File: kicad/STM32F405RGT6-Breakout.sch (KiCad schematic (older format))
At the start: 58 parts, among them J1 USB_C_Receptacle_USB2.0, J2 PWR OUT, J3 SWD/JTAG, J4 USART6, J5 SPI1, J6 I2C1, J7 I2C2, Q1 Si2301CDS, SW1 TS-1187A-B-A-B, SW2 TS-1187A-B-A-B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

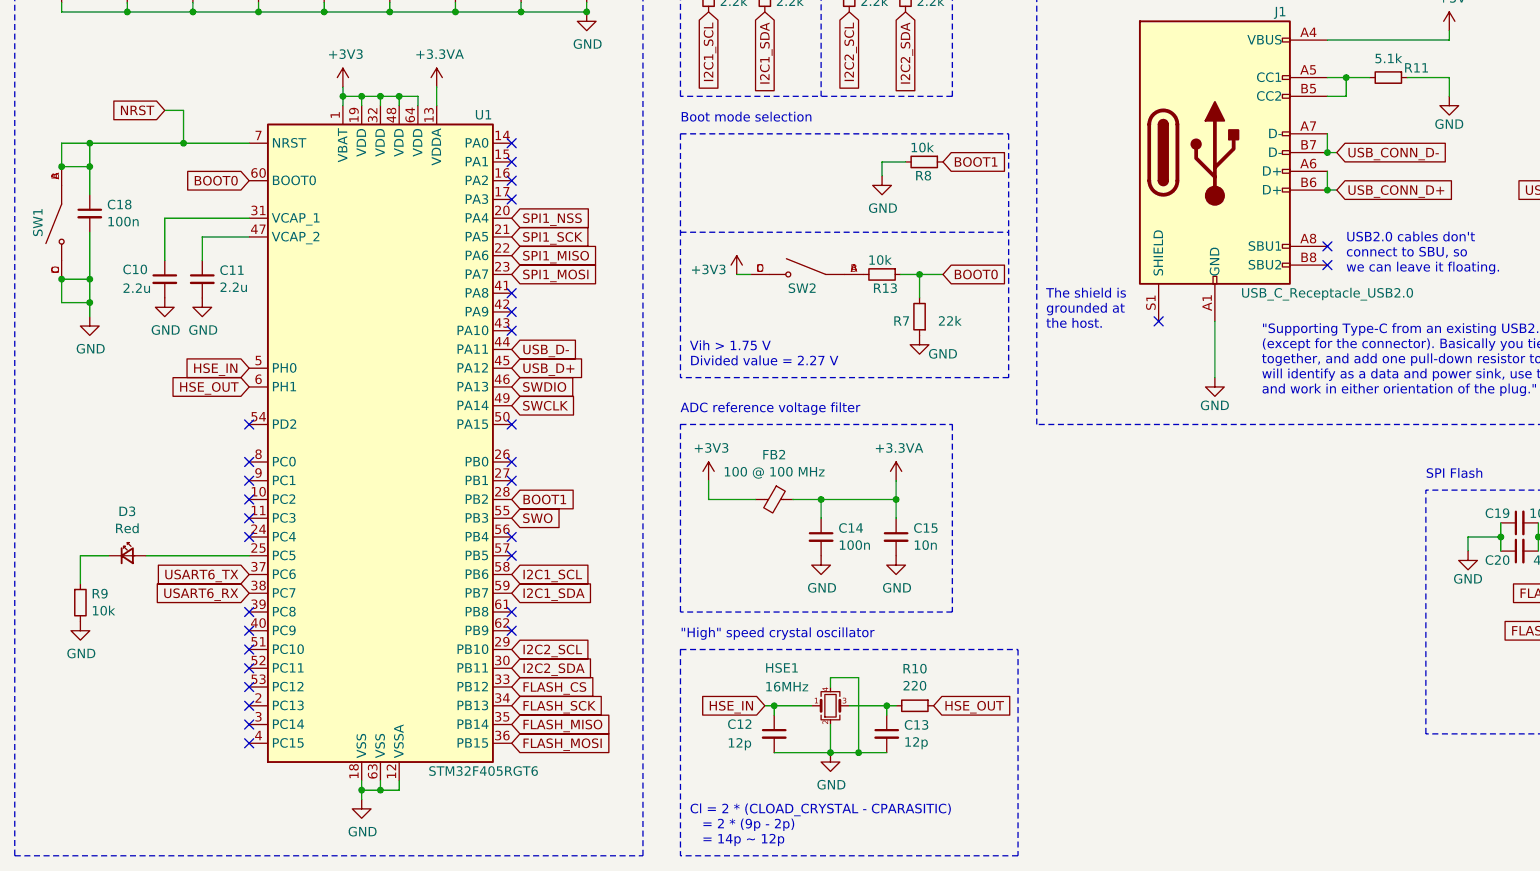
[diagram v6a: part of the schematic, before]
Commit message: - Lots of GPIO breakouts wired up - Lots of signal isolation vias that I'm completely guessing about
Still to lay out and route: power, USB, UART, SWD
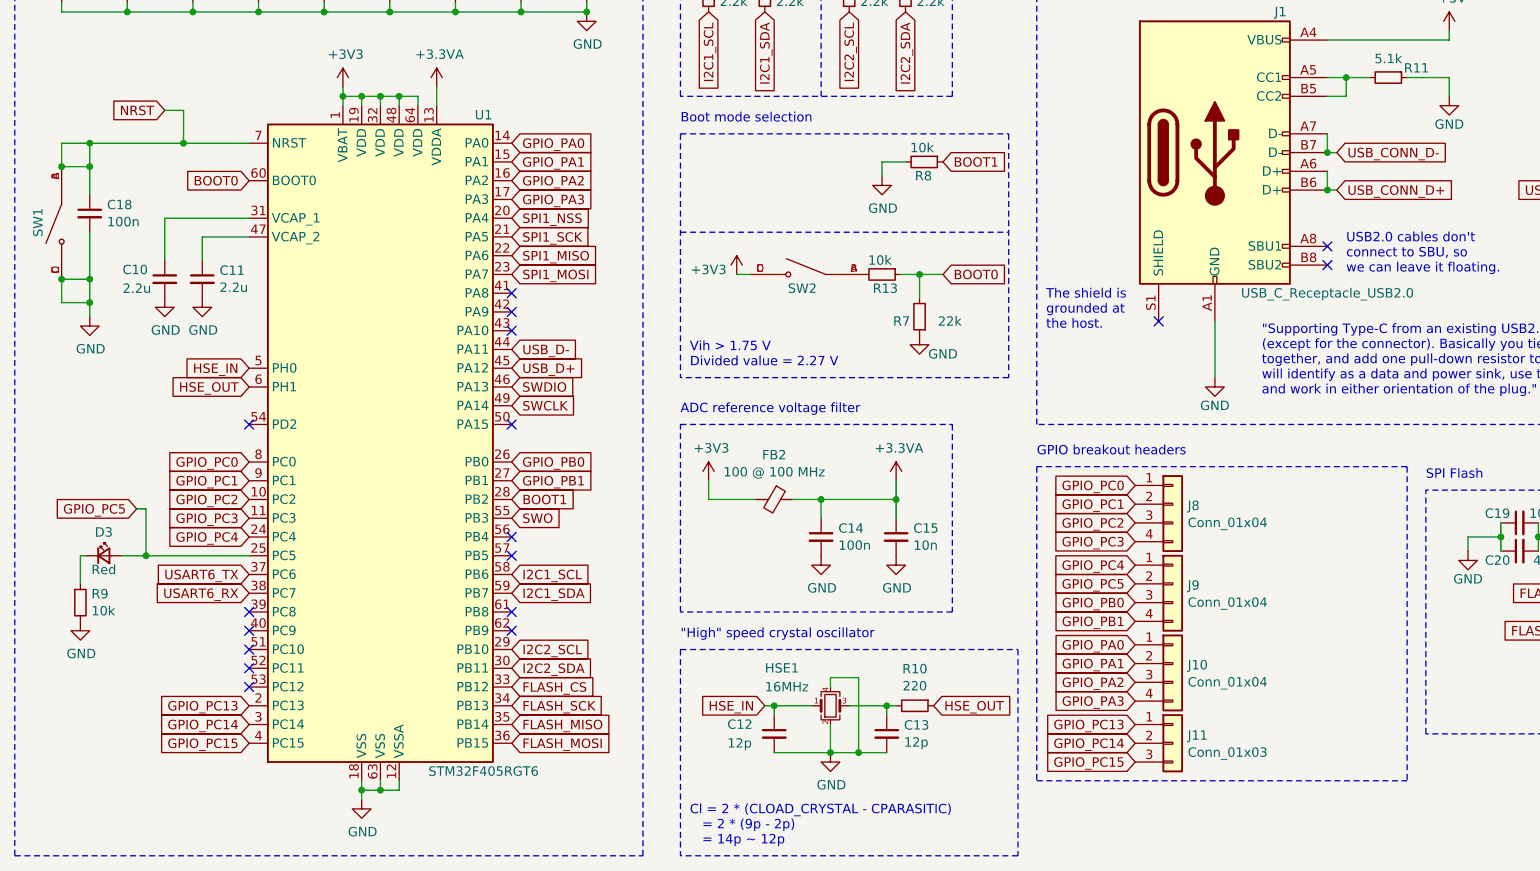
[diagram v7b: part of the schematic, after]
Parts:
- added J10, J8, J9: Conn_01x04, Connector_PinSocket_2.54mm:PinSocket_1x04_P2.54mm_Vertical_SMD_Pin1Left, symbol Connector_Generic:Conn_01x04
- added J11: Conn_01x03, Connector_PinSocket_2.54mm:PinSocket_1x03_P2.54mm_Vertical_SMD_Pin1Left, symbol Connector_Generic:Conn_01x03
- J2: footprint Connector_PinHeader_2.54mm:PinHeader_1x02_P2.54mm_Vertical_SMD_Pin1Left -> Connector_PinSocket_2.54mm:PinSocket_1x02_P2.54mm_Vertical_SMD_Pin1Left
- J4, J5, J6, J7: footprint Connector_PinHeader_2.54mm:PinHeader_1x04_P2.54mm_Vertical_SMD_Pin1Left -> Connector_PinSocket_2.54mm:PinSocket_1x04_P2.54mm_Vertical_SMD_Pin1Left
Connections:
- net GPIO_PC2: now reaches U1.10 (PC2)
- net GPIO_PC2: now also J8.3 (Pin_3)
- net GPIO_PC3: now reaches U1.11 (PC3)
- net GPIO_PC3: now also J8.4 (Pin_4)
- net GPIO_PA0: now reaches U1.14 (PA0)
- net GPIO_PA0: now also J10.1 (Pin_1)
- net GPIO_PA1: now reaches U1.15 (PA1)
- net GPIO_PA1: now also J10.2 (Pin_2)
- net GPIO_PA2: now reaches U1.16 (PA2)
- net GPIO_PA2: now also J10.3 (Pin_3)
- net GPIO_PA3: now reaches U1.17 (PA3)
- net GPIO_PA3: now also J10.4 (Pin_4)
- net GPIO_PC13: now reaches U1.2 (PC13)
- net GPIO_PC13: now also J11.1 (Pin_1)
- net GPIO_PC4: now reaches U1.24 (PC4)
- net GPIO_PC4: now also J9.1 (Pin_1)
- net GPIO_PC5: now reaches D3.2 (A), U1.25 (PC5)
- net GPIO_PC5: now also J9.2 (Pin_2)
- net GPIO_PB0: now reaches U1.26 (PB0)
- net GPIO_PB0: now also J9.3 (Pin_3)
- net GPIO_PB1: now reaches U1.27 (PB1)
- net GPIO_PB1: now also J9.4 (Pin_4)
- net GPIO_PC14: now reaches U1.3 (PC14)
- net GPIO_PC14: now also J11.2 (Pin_2)
- net GPIO_PC15: now reaches U1.4 (PC15)
- net GPIO_PC15: now also J11.3 (Pin_3)
- net GPIO_PC0: now reaches U1.8 (PC0)
- net GPIO_PC0: now also J8.1 (Pin_1)
- net GPIO_PC1: now reaches U1.9 (PC1)
- net GPIO_PC1: now also J8.2 (Pin_2)
- no-connect marks 33 -> 19
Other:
- note added: "GPIO breakout headers"
- moved on the sheet: D3
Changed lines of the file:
@@
 	1000 5900 1000 6050
 Wire Wire Line
-	1150 5900 1000 5900
+	1025 5900 1000 5900
 $Comp
 L Device:LED_Small D3
 U 1 1 61A9A358
-P 1250 5900
-F 0 "D3" H 1250 6135 50  0000 C CNN
-F 1 "Red" H 1250 6044 50  0000 C CNN
-F 2 "Diode_SMD:D_0603_1608Metric" V 1250 5900 50  0001 C CNN
-F 3 "~" V 1250 5900 50  0001 C CNN
-	1    1250 5900
+P 1125 5900
+F 0 "D3" H 1125 6025 50  0000 C CNN
+F 1 "Red" H 1125 5825 50  0000 C CNN
+F 2 "Diode_SMD:D_0603_1608Metric" V 1125 5900 50  0001 C CNN
+F 3 "~" V 1125 5900 50  0001 C CNN
+	1    1125 5900
 	1    0    0    -1
 $EndComp
@@
 NoConn ~ 3300 5900
 NoConn ~ 3300 5800
-NoConn ~ 3300 5500
-NoConn ~ 3300 5400
 NoConn ~ 3300 5200
-NoConn ~ 1900 6900
-NoConn ~ 1900 6800
-NoConn ~ 1900 6700
 NoConn ~ 1900 6600
 NoConn ~ 1900 6500
@@
 NoConn ~ 1900 6300
 NoConn ~ 1900 6200
-NoConn ~ 1900 5800
-NoConn ~ 1900 5700
-NoConn ~ 1900 5600
-NoConn ~ 1900 5500
-NoConn ~ 1900 5400
 NoConn ~ 1900 5200
 NoConn ~ 3300 4700
 NoConn ~ 3300 4600
 NoConn ~ 3300 4500
-NoConn ~ 3300 4000
-NoConn ~ 3300 3900
-NoConn ~ 3300 3800
-NoConn ~ 3300 3700
 Text Notes 875  1775 0    50   ~ 0
 Off when gate is high,\ni.e. supply polarity \nis reversed
@@
 F 0 "J5" H 5650 1900 50  0000 L CNN
 F 1 "SPI1" H 5650 2000 50  0000 L CNN
-F 2 "Connector_PinHeader_2.54mm:PinHeader_1x04_P2.54mm_Vertical_SMD_Pin1Left" H 5550 2000 50  0001 C CNN
+F 2 "Connector_PinSocket_2.54mm:PinSocket_1x04_P2.54mm_Vertical_SMD_Pin1Left" H 5550 2000 50  0001 C CNN
 F 3 "~" H 5550 2000 50  0001 C CNN
 	1    5550 2000
@@
 F 0 "J6" H 5650 1100 50  0000 L CNN
 F 1 "I2C1" H 5650 1200 50  0000 L CNN
-F 2 "Connector_PinHeader_2.54mm:PinHeader_1x04_P2.54mm_Vertical_SMD_Pin1Left" H 5550 1200 50  0001 C CNN
+F 2 "Connector_PinSocket_2.54mm:PinSocket_1x04_P2.54mm_Vertical_SMD_Pin1Left" H 5550 1200 50  0001 C CNN
 F 3 "~" H 5550 1200 50  0001 C CNN
 	1    5550 1200
@@
 F 0 "J7" H 6750 1100 50  0000 L CNN
 F 1 "I2C2" H 6750 1200 50  0000 L CNN
-F 2 "Connector_PinHeader_2.54mm:PinHeader_1x04_P2.54mm_Vertical_SMD_Pin1Left" H 6650 1200 50  0001 C CNN
+F 2 "Connector_PinSocket_2.54mm:PinSocket_1x04_P2.54mm_Vertical_SMD_Pin1Left" H 6650 1200 50  0001 C CNN
 F 3 "~" H 6650 1200 50  0001 C CNN
 	1    6650 1200
@@
 F 0 "J4" H 6750 1850 50  0000 L CNN
 F 1 "USART6" H 6750 1950 50  0000 L CNN
-F 2 "Connector_PinHeader_2.54mm:PinHeader_1x04_P2.54mm_Vertical_SMD_Pin1Left" H 6650 1950 50  0001 C CNN
+F 2 "Connector_PinSocket_2.54mm:PinSocket_1x04_P2.54mm_Vertical_SMD_Pin1Left" H 6650 1950 50  0001 C CNN
 F 3 "~" H 6650 1950 50  0001 C CNN
 	1    6650 1950
@@
 F 0 "J2" H 8500 1050 50  0000 C CNN
 F 1 "PWR OUT" H 8700 1150 50  0000 C CNN
-F 2 "Connector_PinHeader_2.54mm:PinHeader_1x02_P2.54mm_Vertical_SMD_Pin1Left" H 8400 1150 50  0001 C CNN
+F 2 "Connector_PinSocket_2.54mm:PinSocket_1x02_P2.54mm_Vertical_SMD_Pin1Left" H 8400 1150 50  0001 C CNN
 F 3 "~" H 8400 1150 50  0001 C CNN
 	1    8400 1150
@@
 Wire Wire Line
 	7750 3350 7875 3350
+Text GLabel 1900 5500 0    50   Input ~ 0
+GPIO_PC1
+Text GLabel 1900 5600 0    50   Input ~ 0
+GPIO_PC2
+Text GLabel 1900 5700 0    50   Input ~ 0
+GPIO_PC3
+Text GLabel 1900 5400 0    50   Input ~ 0
+GPIO_PC0
+$Comp
+L Connector_Generic:Conn_01x04 J8
+U 1 1 629AE825
+P 6825 5625
+F 0 "J8" H 6905 5617 50  0000 L CNN
+F 1 "Conn_01x04" H 6905 5526 50  0000 L CNN
+F 2 "Connector_PinSocket_2.54mm:PinSocket_1x04_P2.54mm_Vertical_SMD_Pin1Left" H 6825 5625 50  0001 C CNN
+F 3 "~" H 6825 5625 50  0001 C CNN
+	1    6825 5625
+	1    0    0    -1
+$EndComp
+Text GLabel 6625 5625 0    50   Input ~ 0
+GPIO_PC1
+Text GLabel 6625 5725 0    50   Input ~ 0
+GPIO_PC2
+Text GLabel 6625 5825 0    50   Input ~ 0
+GPIO_PC3
+Text GLabel 6625 5525 0    50   Input ~ 0
+GPIO_PC0
+Text GLabel 1900 5800 0    50   Input ~ 0
+GPIO_PC4
+Text GLabel 1300 5650 0    50   Input ~ 0
+GPIO_PC5
+Wire Wire Line
+	1300 5650 1350 5650
+Wire Wire Line
+	1350 5650 1350 5900
+Connection ~ 1350 5900
+Wire Wire Line
+	1350 5900 1225 5900
+$Comp
+L Connector_Generic:Conn_01x04 J9
+U 1 1 629DD192
+P 6825 6050
+F 0 "J9" H 6905 6042 50  0000 L CNN
+F 1 "Conn_01x04" H 6905 5951 50  0000 L CNN
+F 2 "Connector_PinSocket_2.54mm:PinSocket_1x04_P2.54mm_Vertical_SMD_Pin1Left" H 6825 6050 50  0001 C CNN
+F 3 "~" H 6825 6050 50  0001 C CNN
+	1    6825 6050
+	1    0    0    -1
+$EndComp
+Text GLabel 6625 6050 0    50   Input ~ 0
+GPIO_PC5
+Text GLabel 6625 6150 0    50   Input ~ 0
+GPIO_PB0
+Text GLabel 6625 6250 0    50   Input ~ 0
+GPIO_PB1
+Text GLabel 6625 5950 0    50   Input ~ 0
+GPIO_PC4
+Text GLabel 3300 5400 2    50   Input ~ 0
+GPIO_PB0
+Text GLabel 3300 5500 2    50   Input ~ 0
+GPIO_PB1
+$Comp
+L Connector_Generic:Conn_01x04 J10
+U 1 1 62A179BD
+P 6825 6475
+F 0 "J10" H 6905 6467 50  0000 L CNN
+F 1 "Conn_01x04" H 6905 6376 50  0000 L CNN
+F 2 "Connector_PinSocket_2.54mm:PinSocket_1x04_P2.54mm_Vertical_SMD_Pin1Left" H 6825 6475 50  0001 C CNN
+F 3 "~" H 6825 6475 50  0001 C CNN
+	1    6825 6475
+	1    0    0    -1
+$EndComp
+Text GLabel 6625 6475 0    50   Input ~ 0
+GPIO_PA1
+Text GLabel 6625 6575 0    50   Input ~ 0
+GPIO_PA2
+Text GLabel 6625 6675 0    50   Input ~ 0
+GPIO_PA3
+Text GLabel 6625 6375 0    50   Input ~ 0
+GPIO_PA0
+Text GLabel 3300 3800 2    50   Input ~ 0
+GPIO_PA1
+Text GLabel 3300 3900 2    50   Input ~ 0
+GPIO_PA2
+Text GLabel 3300 4000 2    50   Input ~ 0
+GPIO_PA3
+Text GLabel 3300 3700 2    50   Input ~ 0
+GPIO_PA0
+$Comp
+L Connector_Generic:Conn_01x03 J11
+U 1 1 62A3C530
+P 6825 6900
+F 0 "J11" H 6905 6942 50  0000 L CNN
+F 1 "Conn_01x03" H 6905 6851 50  0000 L CNN
+F 2 "Connector_PinSocket_2.54mm:PinSocket_1x03_P2.54mm_Vertical_SMD_Pin1Left" H 6825 6900 50  0001 C CNN
+F 3 "~" H 6825 6900 50  0001 C CNN
+	1    6825 6900
+	1    0    0    -1
+$EndComp
+Text GLabel 6625 6800 0    50   Input ~ 0
+GPIO_PC13
+Text GLabel 6625 6900 0    50   Input ~ 0
+GPIO_PC14
+Text GLabel 6625 7000 0    50   Input ~ 0
+GPIO_PC15
+Text GLabel 1900 6700 0    50   Input ~ 0
+GPIO_PC13
+Text GLabel 1900 6800 0    50   Input ~ 0
+GPIO_PC14
+Text GLabel 1900 6900 0    50   Input ~ 0
+GPIO_PC15
+Wire Notes Line
+	8075 5425 6100 5425
+Wire Notes Line
+	8075 5425 8075 7100
+Wire Notes Line
+	6100 7100 8075 7100
+Wire Notes Line
+	6100 5425 6100 7100
+Text Notes 6100 5375 0    50   ~ 0
+GPIO breakout headers
 $EndSCHEMATC

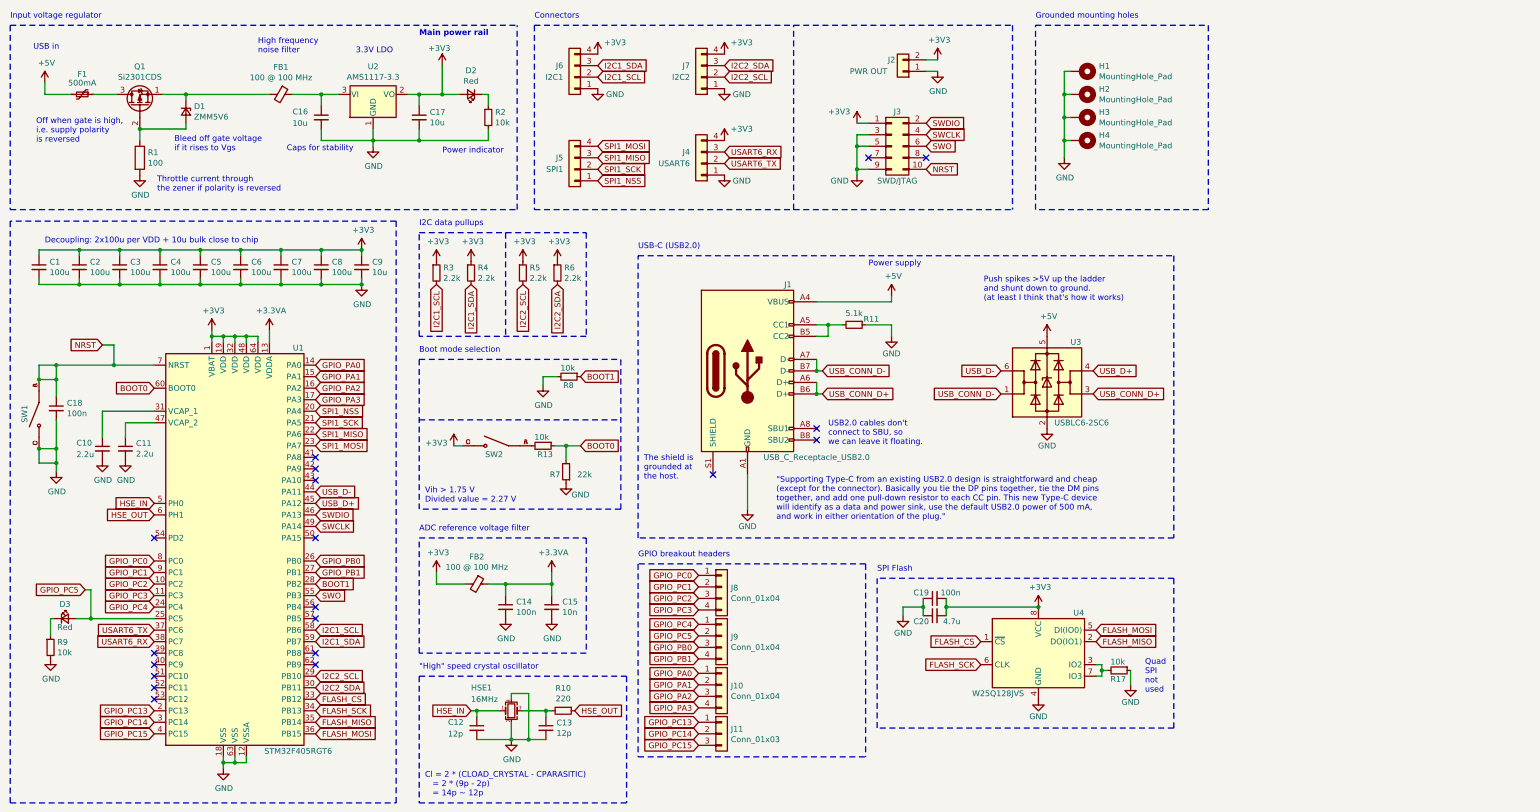
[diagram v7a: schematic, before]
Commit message: Adopting the constraint of Arduino Uno shield compatibility to narrow the design choices a bit
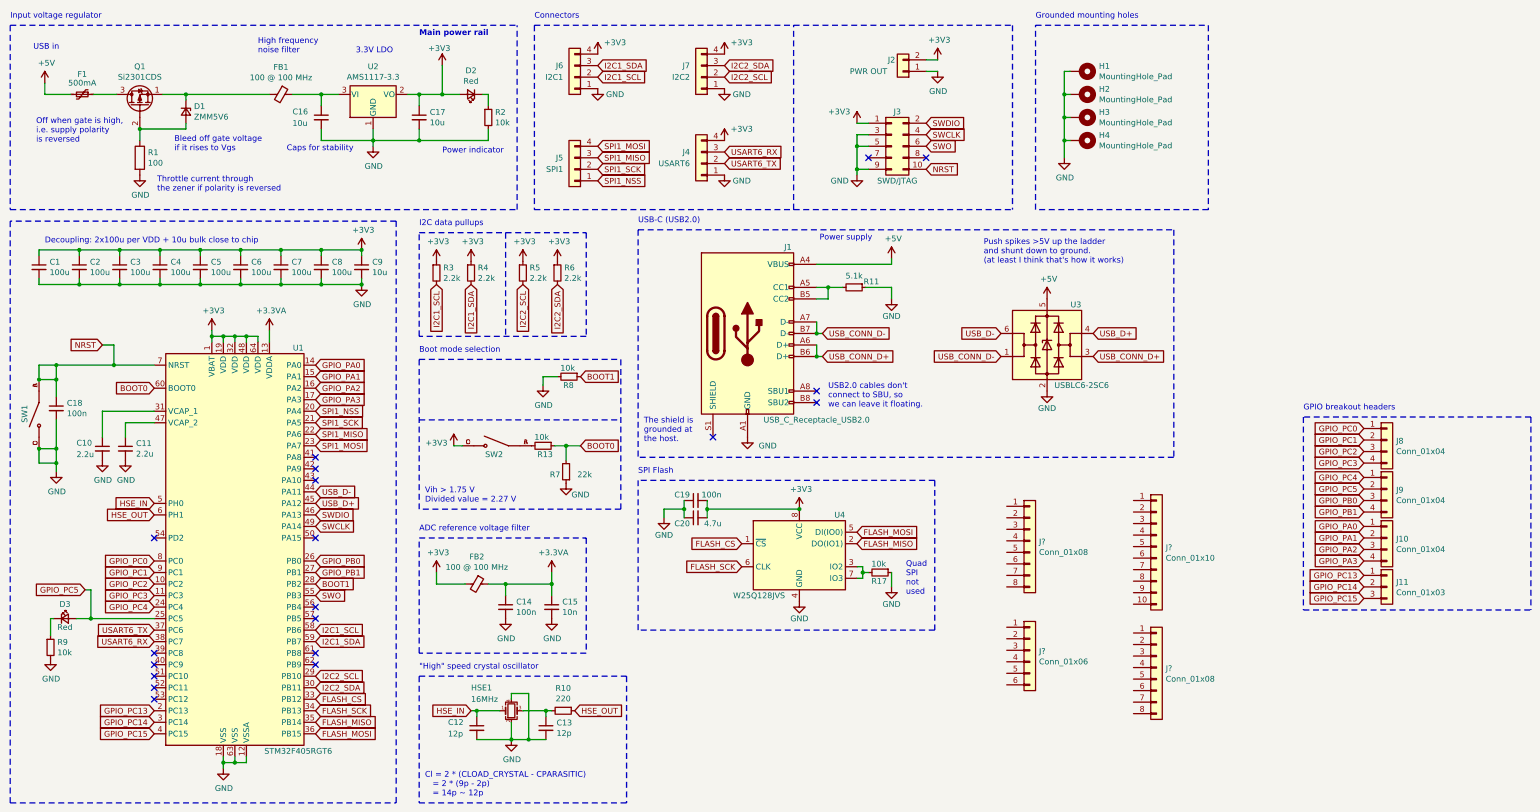
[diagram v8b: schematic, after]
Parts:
- added J? (x2): Conn_01x08, symbol Connector_Generic:Conn_01x08
- added J?: Conn_01x10, symbol Connector_Generic:Conn_01x10
- added J?: Conn_01x06, symbol Connector_Generic:Conn_01x06
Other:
- note removed: ""Supporting Type-C from an existing USB2.0 design is straightforward and cheap \n(except for the connector). Basically you tie the DP pins together, tie the DM pins \ntogether, and add one pull-down resistor to each CC pin. This new Type-C device \nwill identify as a data and power sink, use the default USB2.0 power of 500 mA, \nand work in either orientation of the plug.""
- moved on the sheet: C19, C20, J1, J10, J11, J8, J9, R11, R17, U3, U4
